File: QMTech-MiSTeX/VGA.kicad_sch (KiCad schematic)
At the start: 8 parts, among them J10 Conn_01x02

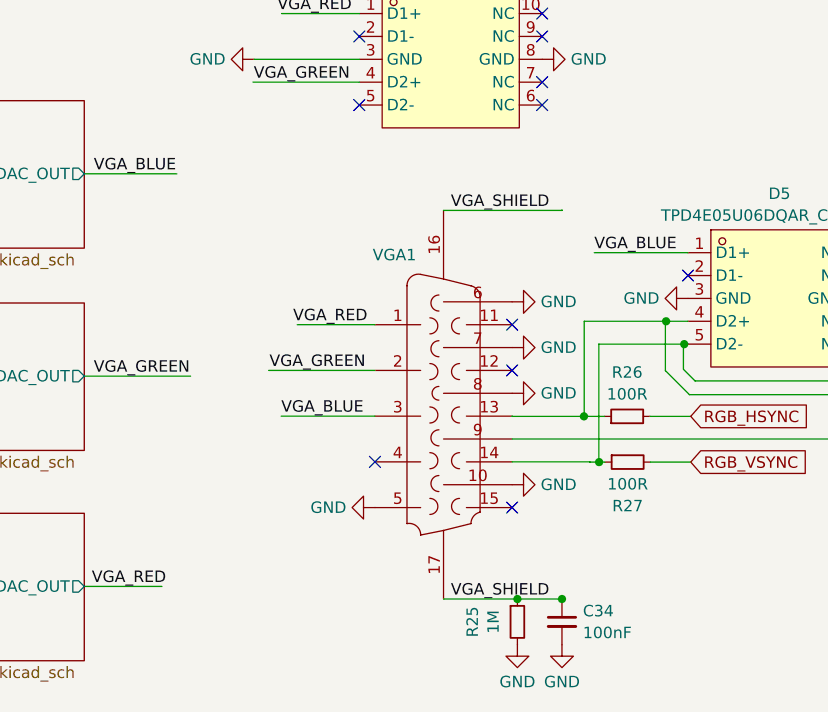
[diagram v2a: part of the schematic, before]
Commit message: add test points for VGA signals
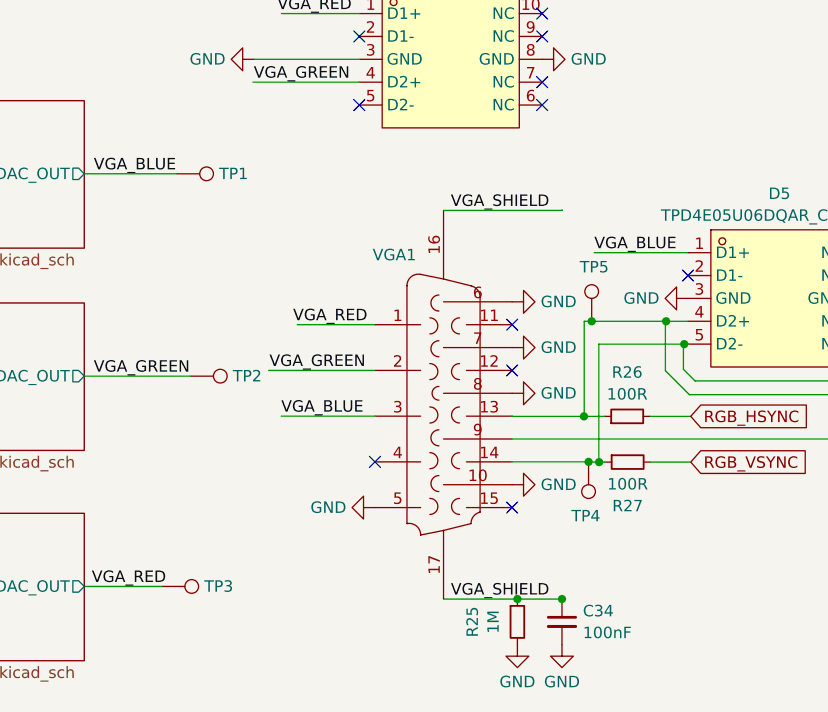
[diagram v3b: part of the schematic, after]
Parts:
- added TP1, TP2, TP3: TestPoint, TestPoint:TestPoint_Pad_D2.0mm, symbol Connector:TestPoint
- added TP4, TP5: TestPoint, TestPoint:TestPoint_Pad_D1.5mm, symbol Connector:TestPoint
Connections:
- net VGA_BLUE: now also TP1.1
- net VGA_GREEN: now also TP2.1
- net VGA_RED: now also TP3.1
- net at D5.4 (D2+), D5.7 (NC), R26.1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: now also TP5.1
- net at D5.5 (D2-), D5.6 (NC), R27.1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: now also TP4.1
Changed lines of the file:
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@@
   (junction (at 160.143 124.46) (diameter 0) (color 0 0 0 0)
   )
+  (junction (at 160.6536 129.5146) (diameter 0) (color 0 0 0 0)
+  )
   (junction (at 161.8234 129.54) (diameter 0) (color 0 0 0 0)
   )
@@
   (junction (at 171.2841 116.4336) (diameter 0) (color 0 0 0 0)
   )
+  (junction (at 161.0018 113.8936) (diameter 0) (color 0 0 0 0)
+  )
   (no_connect (at 171.704 108.8136))
   (no_connect (at 155.4988 82.2452))
@@
     (stroke (width 0) (type default))
   )
-  (wire (pts (xy 160.1763 113.8936) (xy 169.2694 113.8936))
+  (wire (pts (xy 160.1763 113.8936) (xy 161.0018 113.8936))
     (stroke (width 0) (type default))
   )
@@
     (stroke (width 0) (type default))
   )
+  (wire (pts (xy 161.0018 113.8936) (xy 169.2694 113.8936))
+    (stroke (width 0) (type default))
+  )
   (wire (pts (xy 152.1599 124.46) (xy 152.1599 124.4346))
     (stroke (width 0) (type default))
@@
     (stroke (width 0) (type default))
   )
-  (wire (pts (xy 152.1599 129.5146) (xy 160.782 129.5146))
+  (wire (pts (xy 152.1599 129.5146) (xy 160.6536 129.5146))
     (stroke (width 0) (type default))
   )
@@
     (stroke (width 0) (type default))
   )
+  (wire (pts (xy 160.6536 129.5146) (xy 160.782 129.5146))
+    (stroke (width 0) (type default))
+  )
   (wire (pts (xy 56.4896 113.7666) (xy 79.6036 113.7666))
     (stroke (width 0) (type default))
@@
     )
   )
+  (symbol (lib_id "Connector:TestPoint") (at 160.6536 129.5146 180) (unit 1)
+    (in_bom yes) (on_board yes) (dnp no)
+    (property "Reference" "TP4" (at 158.75 135.5344 0)
+      (effects (font (size 1.27 1.27)) (justify right))
+    )
+    (property "Value" "TestPoint" (at 159.4415 134.2136 90)
+      (effects (font (size 1.27 1.27)) (justify left) hide)
+    )
+    (property "Footprint" "TestPoint:TestPoint_Pad_D1.5mm" (at 155.5736 129.5146 0)
+      (effects (font (size 1.27 1.27)) hide)
+    )
+    (property "Datasheet" "~" (at 155.5736 129.5146 0)
+      (effects (font (size 1.27 1.27)) hide)
+    )
+    (pin "1")
+    (instances
+      (project "QMTech-MiSTeX"
+        (path "/bf95850e-2fcb-4784-a603-f17fc357556b/8c1d97fc-c85e-4afc-840e-7429a199eff3"
+          (reference "TP4") (unit 1)
+        )
+      )
+    )
+  )
+  (symbol (lib_id "Connector:TestPoint") (at 114.9096 97.5106 270) (unit 1)
+    (in_bom yes) (on_board yes) (dnp no) (fields_autoplaced)
+    (property "Reference" "TP1" (at 119.6086 97.5106 90)
+      (effects (font (size 1.27 1.27)) (justify left))
+    )
+    (property "Value" "TestPoint" (at 119.6086 98.7227 90)
+      (effects (font (size 1.27 1.27)) (justify left) hide)
+    )
+    (property "Footprint" "TestPoint:TestPoint_Pad_D2.0mm" (at 114.9096 102.5906 0)
+      (effects (font (size 1.27 1.27)) hide)
+    )
+    (property "Datasheet" "~" (at 114.9096 102.5906 0)
+      (effects (font (size 1.27 1.27)) hide)
+    )
+    (pin "1")
+    (instances
+      (project "QMTech-MiSTeX"
+        (path "/bf95850e-2fcb-4784-a603-f17fc357556b/8c1d97fc-c85e-4afc-840e-7429a199eff3"
+          (reference "TP1") (unit 1)
+        )
+      )
+    )
+  )
+  (symbol (lib_id "Connector:TestPoint") (at 113.2586 143.3576 270) (unit 1)
+    (in_bom yes) (on_board yes) (dnp no) (fields_autoplaced)
+    (property "Reference" "TP3" (at 117.9576 143.3576 90)
+      (effects (font (size 1.27 1.27)) (justify left))
+    )
+    (property "Value" "TestPoint" (at 117.9576 144.5697 90)
+      (effects (font (size 1.27 1.27)) (justify left) hide)
+    )
+    (property "Footprint" "TestPoint:TestPoint_Pad_D2.0mm" (at 113.2586 148.4376 0)
+      (effects (font (size 1.27 1.27)) hide)
+    )
+    (property "Datasheet" "~" (at 113.2586 148.4376 0)
+      (effects (font (size 1.27 1.27)) hide)
+    )
+    (pin "1")
+    (instances
+      (project "QMTech-MiSTeX"
+        (path "/bf95850e-2fcb-4784-a603-f17fc357556b/8c1d97fc-c85e-4afc-840e-7429a199eff3"
+          (reference "TP3") (unit 1)
+        )
+      )
+    )
+  )
   (symbol (lib_id "jlcpcb-basic-mlcc-0402:100nF") (at 157.7007 147.2946 0) (unit 1)
     (in_bom yes) (on_board yes) (dnp no)
@@
         )
       )
+    )
+  )
+  (symbol (lib_id "Connector:TestPoint") (at 116.4336 119.9896 270) (unit 1)
+    (in_bom yes) (on_board yes) (dnp no) (fields_autoplaced)
+    (property "Reference" "TP2" (at 121.1326 119.9896 90)
+      (effects (font (size 1.27 1.27)) (justify left))
+    )
+    (property "Value" "TestPoint" (at 121.1326 121.2017 90)
+      (effects (font (size 1.27 1.27)) (justify left) hide)
+    )
+    (property "Footprint" "TestPoint:TestPoint_Pad_D2.0mm" (at 116.4336 125.0696 0)
+      (effects (font (size 1.27 1.27)) hide)
+    )
+    (property "Datasheet" "~" (at 116.4336 125.0696 0)
+      (effects (font (size 1.27 1.27)) hide)
+    )
+    (pin "1")
+    (instances
+      (project "QMTech-MiSTeX"
+        (path "/bf95850e-2fcb-4784-a603-f17fc357556b/8c1d97fc-c85e-4afc-840e-7429a199eff3"
+          (reference "TP2") (unit 1)
+        )
+      )
+    )
+  )
+  (symbol (lib_id "Connector:TestPoint") (at 161.0018 113.8936 0) (unit 1)
+    (in_bom yes) (on_board yes) (dnp no)
+    (property "Reference" "TP5" (at 162.9054 107.8738 0)
+      (effects (font (size 1.27 1.27)) (justify right))
+    )
+    (property "Value" "TestPoint" (at 162.2139 109.1946 90)
+      (effects (font (size 1.27 1.27)) (justify left) hide)
+    )
+    (property "Footprint" "TestPoint:TestPoint_Pad_D1.5mm" (at 166.0818 113.8936 0)
+      (effects (font (size 1.27 1.27)) hide)
+    )
+    (property "Datasheet" "~" (at 166.0818 113.8936 0)
+      (effects (font (size 1.27 1.27)) hide)
+    )
+    (pin "1")
+    (instances
+      (project "QMTech-MiSTeX"
+        (path "/bf95850e-2fcb-4784-a603-f17fc357556b/8c1d97fc-c85e-4afc-840e-7429a199eff3"
+          (reference "TP5") (unit 1)
+        )
+      )

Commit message: power filtering, testpoints, bottom caps, more decoupling, teardrops
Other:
- title: (none) -> VGA Video Output
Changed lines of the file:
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@@
 (kicad_sch (version 20230121) (generator eeschema)
   (paper "A4")
+  (title_block
+    (title "VGA Video Output")
+  )
   (junction (at 152.7482 144.7546) (diameter 0) (color 0 0 0 0)
   )

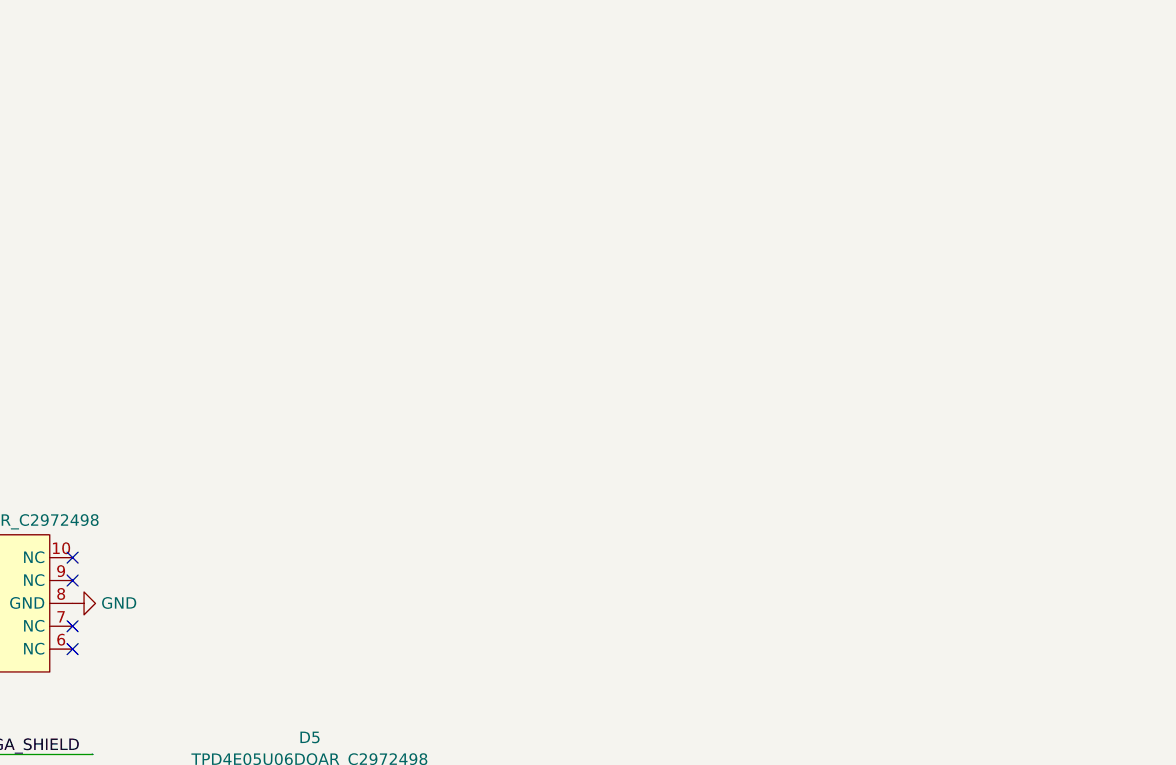
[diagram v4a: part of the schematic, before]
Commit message: Add VGA green probe, add DIP switches, add to silk screen, cosmetics
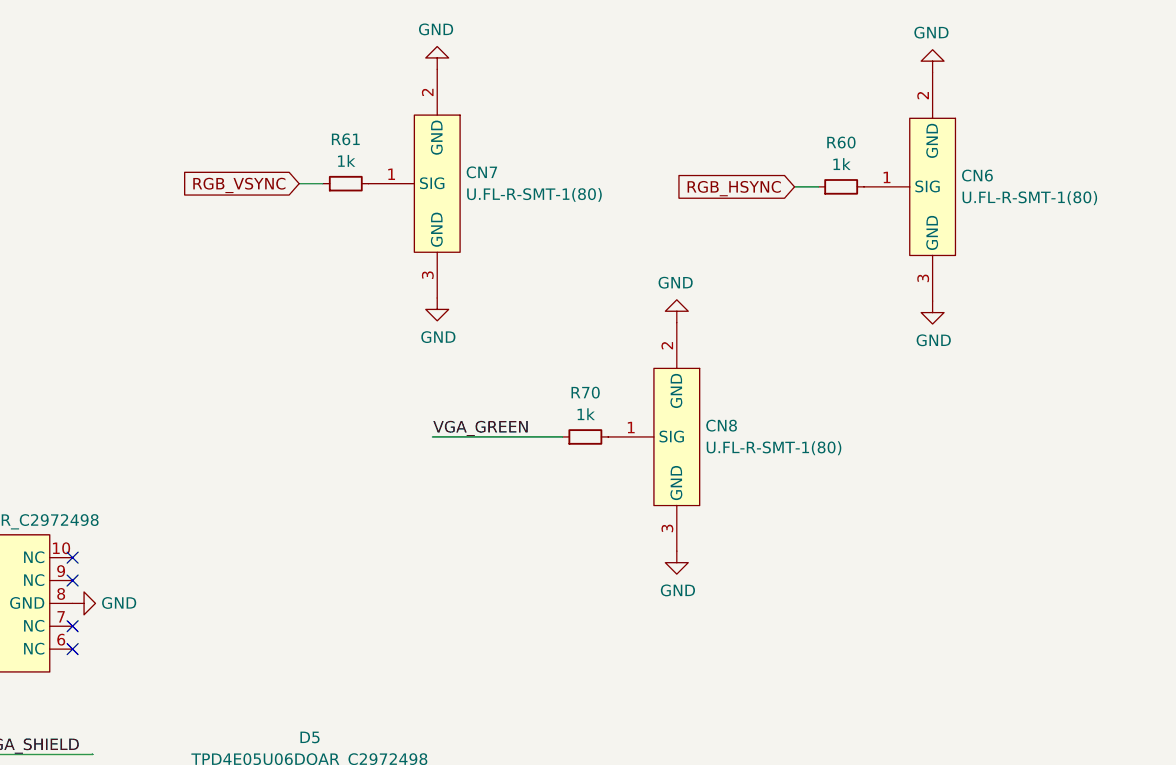
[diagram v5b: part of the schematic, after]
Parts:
- added CN6, CN7, CN8: U.FL-R-SMT-1(80), easyeda2kicad:RF-SMD_FRF05002-JSS103M, symbol easyeda2kicad:U.FL-R-SMT-1(80)
- added R60, R61, R70: 1k, R_0402_1005Metric, symbol jlcpcb-basic-resistor-0402:1k
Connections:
- net GND: now also CN6.2 (GND), CN6.3 (GND), CN7.2 (GND), CN7.3 (GND), CN8.2 (GND), CN8.3 (GND)
- net RGB_HSYNC: now also R60.1
- net RGB_VSYNC: now also R61.1
- net VGA_GREEN: now also R70.1
- new net: CN6.1 (SIG), R60.2
- new net: CN8.1 (SIG), R70.2
- new net: CN7.1 (SIG), R61.2
